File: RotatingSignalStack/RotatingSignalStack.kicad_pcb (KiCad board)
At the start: 2 copper layers, 4.1 x 4.1 mm, 94 parts, among them IC2 STM32H562RIT6, J2 Conn_ARM_SWD_TagConnect_TC203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, J3 RJ45_LED_Shielded, SW1 SW_Push, SW2 Boot Switch, SW3 SW_Push, SW4 SW_Push, SW8 SW_Push, T1 GMG116S1202R, U1 TMAG5273C1QDBVR, U2 AP63203WU-7, U3 SN65HVD232, U4 DP83825I, U5 SG-210STF 50.0000ML0, U6 USBLC6-2SC6, U7 USBLC6-4SC6

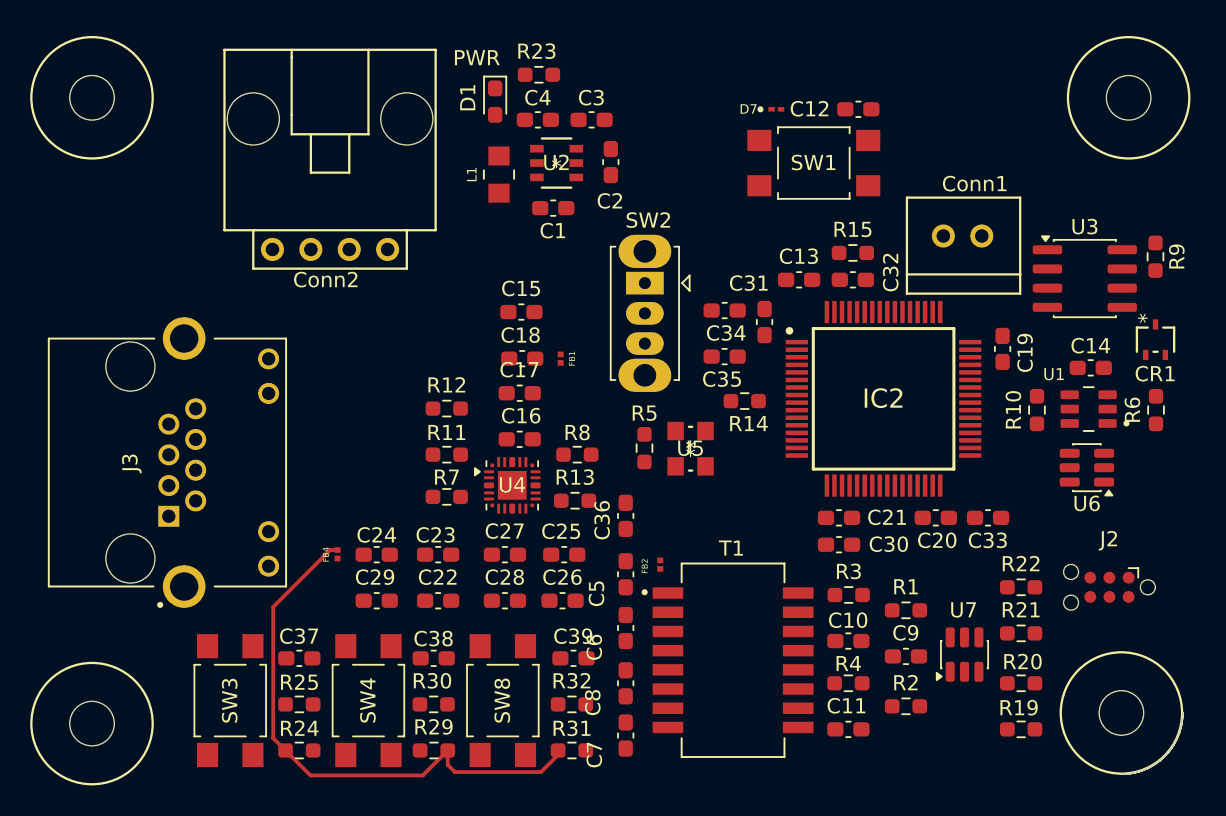
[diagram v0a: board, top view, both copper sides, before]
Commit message: mounting hole fix
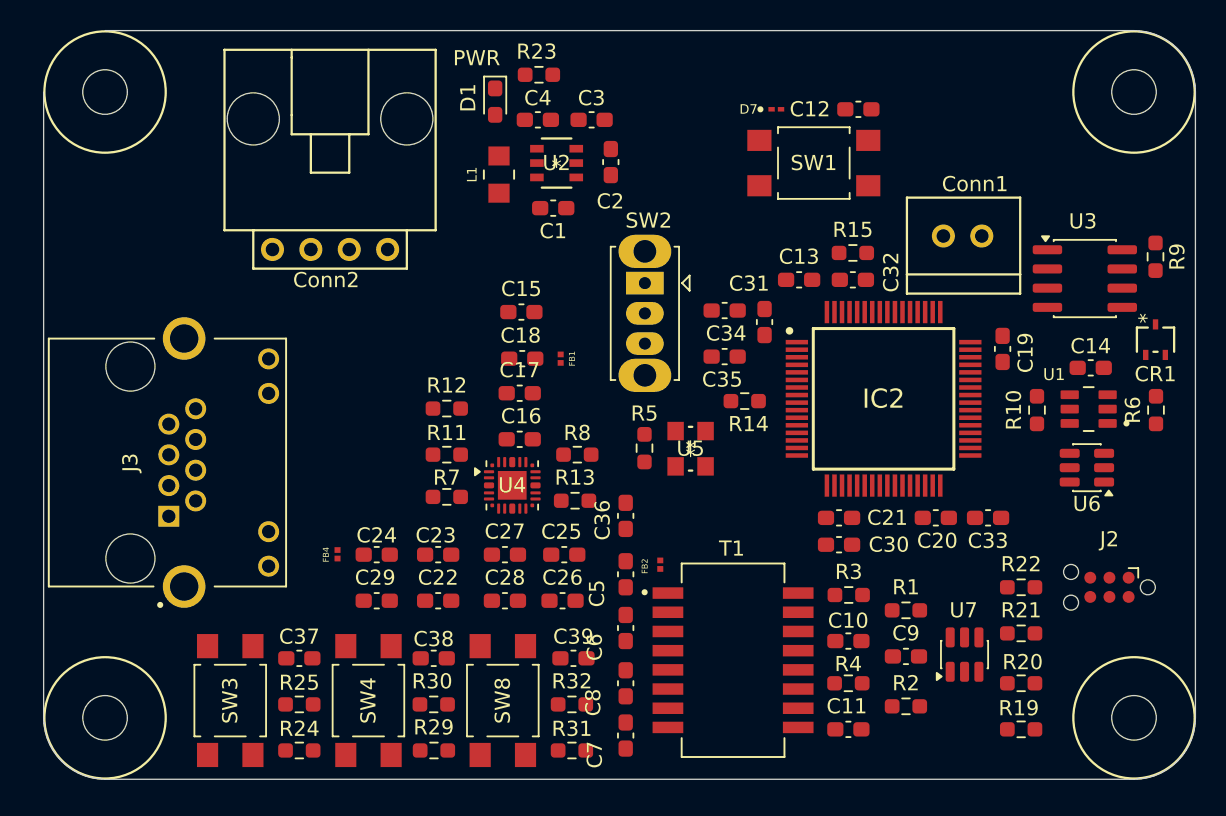
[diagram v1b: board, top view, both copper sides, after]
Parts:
- moved H1 69.3 mm to (179.9, 115.1), turned to -90 degrees
- moved H4 59.2 mm to (119.8, 115.1), turned to 180 degrees
- moved H2 33.8 mm to (119.8, 81.7), turned to 90 degrees
- moved H3 0.52 mm to (179.9, 81.7)
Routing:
- net VBAT: track 37.0 -> 0.29 mm
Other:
- board size 4.1 x 4.1 mm -> 76.2 x 49.5 mm
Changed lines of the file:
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@@
 	(footprint "MRDT_Drill_Holes:4_40_Hole_Corner"
 		(layer "F.Cu")
-		(at 118.96962 82.11312 90)
+		(at 179.88788 115.11788 -90)
 		(property "Reference" "H1"
 			(at 4.00812 -3.50812 90)
@@
 		)
 		(fp_line
-			(start 4.0132 -8.0264)
-			(end 0 -8.0264)
+			(start 0 0)
+			(end 8.0264 0)
 			(stroke
 				(width 0.15)
@@
 		)
 		(fp_line
-			(start 0 -8.0264)
-			(end 0 0)
+			(start 8.0264 -4.0132)
+			(end 8.0264 0)
 			(stroke
 				(width 0.15)
@@
 		)
 		(fp_line
-			(start 8.0264 -4.0132)
-			(end 8.0264 0)
+			(start 0 -8.0264)
+			(end 0 0)
 			(stroke
 				(width 0.15)
@@
 		)
 		(fp_line
-			(start 0 0)
-			(end 8.0264 0)
+			(start 4.0132 -8.0264)
+			(end 0 -8.0264)
 			(stroke
 				(width 0.15)
@@
 		)
 		(pad "" np_thru_hole circle
-			(at 4.00812 -4.00812 90)
+			(at 4.00812 -4.00812 270)
 			(size 2.9464 2.9464)
 			(drill 2.9464)
@@
 		)
 		(fp_text user "${REFERENCE}"
-			(at -1.524 -4.9295 90)
+			(at -0.1005 0 180)
 			(layer "F.Fab")
 			(effects
@@
 		(tags "SOIC SO")
 		(property "Reference" "U3"
-			(at 0 -3.4 0)
+			(at -0.127 -3.781 0)
 			(layer "F.SilkS")
 			(effects
@@
 	(footprint "MRDT_Drill_Holes:4_40_Hole_Corner"
 		(layer "F.Cu")
-		(at 179.53338 82.11312)
+		(at 179.88788 81.73212)
 		(property "Reference" "H3"
 			(at 4.00812 -3.50812 0)
@@
 	(footprint "MRDT_Drill_Holes:4_40_Hole_Corner"
 		(layer "F.Cu")
-		(at 179.0559 114.7939 -90)
+		(at 119.83212 115.11788 180)
 		(property "Reference" "H4"
-			(at 4.00812 -3.50812 90)
+			(at 4.00812 -3.50812 0)
 			(layer "F.SilkS")
 			(hide yes)
@@
 		)
 		(property "Value" "MountingHole"
-			(at 4.00812 -4.50812 90)
+			(at 4.00812 -4.50812 0)
 			(layer "F.Fab")
 			(hide yes)
@@
 		)
 		(property "Datasheet" "~"
-			(at 0 0 90)
+			(at 0 0 0)
 			(layer "F.Fab")
 			(hide yes)
@@
 		)
 		(property "Description" "Mounting Hole without connection"
-			(at 0 0 90)
+			(at 0 0 0)
 			(layer "F.Fab")
 			(hide yes)
@@
 		)
 		(fp_line
-			(start 0 0)
+			(start 8.0264 -4.0132)
 			(end 8.0264 0)
 			(stroke
@@
 		)
 		(fp_line
-			(start 8.0264 -4.0132)
-			(end 8.0264 0)
+			(start 4.0132 -8.0264)
+			(end 0 -8.0264)
 			(stroke
 				(width 0.15)
@@
 		)
 		(fp_line
-			(start 0 -8.0264)
-			(end 0 0)
+			(start 0 0)
+			(end 8.0264 0)
 			(stroke
 				(width 0.15)
@@
 		)
 		(fp_line
-			(start 4.0132 -8.0264)
-			(end 0 -8.0264)
+			(start 0 -8.0264)
+			(end 0 0)
 			(stroke
 				(width 0.15)
@@
 		)
 		(pad "" np_thru_hole circle
-			(at 4.00812 -4.00812 270)
+			(at 4.00812 -4.00812 180)
 			(size 2.9464 2.9464)
 			(drill 2.9464)
@@
 	(footprint "MRDT_Drill_Holes:4_40_Hole_Corner"
 		(layer "F.Cu")
-		(at 118.96962 115.49888 180)
+		(at 119.83212 81.73212 90)
 		(property "Reference" "H2"
-			(at 4.00812 -3.50812 0)
+			(at 4.00812 -3.50812 90)
 			(layer "F.SilkS")
 			(hide yes)
@@
 		)
 		(property "Value" "MountingHole"
-			(at 4.00812 -4.50812 0)
+			(at 4.00812 -4.50812 90)
 			(layer "F.Fab")
 			(hide yes)
@@
 		)
 		(property "Datasheet" "~"
-			(at 0 0 0)
+			(at 0 0 90)
 			(layer "F.Fab")
 			(hide yes)
@@
 		)
 		(property "Description" "Mounting Hole without connection"
-			(at 0 0 0)
+			(at 0 0 90)
 			(layer "F.Fab")
 			(hide yes)
@@
 		)
 		(fp_line
-			(start 8.0264 -4.0132)
-			(end 8.0264 0)
+			(start 4.0132 -8.0264)
+			(end 0 -8.0264)
 			(stroke
 				(width 0.15)
@@
 		)
 		(fp_line
-			(start 4.0132 -8.0264)
-			(end 0 -8.0264)
+			(start 0 -8.0264)
+			(end 0 0)
 			(stroke
 				(width 0.15)
@@
 		)
 		(fp_line
-			(start 0 0)
+			(start 8.0264 -4.0132)
 			(end 8.0264 0)
 			(stroke
@@
 		)
 		(fp_line
-			(start 0 -8.0264)
-			(end 0 0)
+			(start 0 0)
+			(end 8.0264 0)
 			(stroke
 				(width 0.15)
@@
 		)
 		(pad "" np_thru_hole circle
-			(at 4.00812 -4.00812 180)
+			(at 4.00812 -4.00812 90)
 			(size 2.9464 2.9464)
 			(drill 2.9464)
@@
 	)
 	(gr_arc
-		(start 187.12802 118.80202)
-		(mid 185.937702 121.675702)
-		(end 183.06402 122.86602)
+		(start 115.824 123.19)
+		(mid 112.950318 121.999682)
+		(end 111.76 119.126)
 		(stroke
 			(width 0.05)
@@
 	)
 	(gr_arc
-		(start 187.12802 118.80202)
-		(mid 185.937702 121.675702)
-		(end 183.06402 122.86602)
+		(start 183.896 73.66)
+		(mid 186.769682 74.850318)
+		(end 187.96 77.724)
 		(stroke
 			(width 0.05)
@@
 		(layer "Edge.Cuts")
 	)
-	(gr_arc
-		(start 187.12802 118.80202)
-		(mid 185.937702 121.675702)
-		(end 183.06402 122.86602)
+	(gr_line
+		(start 115.824 123.19)
+		(end 183.896 123.19)
+		(stroke
+			(width 0.05)
+			(type default)
+		)
+		(layer "Edge.Cuts")
+	)
+	(gr_line
+		(start 183.896 73.66)
+		(end 115.824 73.66)
+		(stroke
+			(width 0.05)
+			(type default)
+		)
+		(layer "Edge.Cuts")
+	)
+	(gr_line
+		(start 187.96 119.126)
+		(end 187.96 77.724)
+		(stroke
+			(width 0.05)
+			(type default)
+		)
+		(layer "Edge.Cuts")
+	)
+	(gr_line
+		(start 111.76 77.724)
+		(end 111.76 119.126)
 		(stroke
 			(width 0.05)
@@
 	)
 	(gr_arc
-		(start 187.12802 118.80202)
-		(mid 185.937702 121.675702)
-		(end 183.06402 122.86602)
+		(start 187.96 119.126)
+		(mid 186.769682 121.999682)
+		(end 183.896 123.19)
 		(stroke
 			(width 0.05)
@@
 	)
 	(segment
-		(start 145.799 121.5795)
-		(end 144.6675 122.711)
-		(width 0.254)
-		(layer "F.Cu")
-		(net 6)
-	)
-	(segment
-		(start 138.495224 122.239224)
-		(end 138.495224 121.285)
-		(width 0.254)
-		(layer "F.Cu")
-		(net 6)
-	)
-	(segment
-		(start 126.9495 120.4695)
-		(end 126.9495 111.7935)
-		(width 0.254)
-		(layer "F.Cu")
-		(net 6)
-	)
-	(segment
-		(start 127.765 121.285)
-		(end 126.9495 120.4695)
-		(width 0.254)
-		(layer "F.Cu")
-		(net 6)
-	)
-	(segment
-		(start 129.416 122.936)
-		(end 127.765 121.285)
-		(width 0.254)
-		(layer "F.Cu")
-		(net 6)
-	)
-	(segment
-		(start 138.967 122.711)
-		(end 138.495224 122.239224)
-		(width 0.254)
-		(layer "F.Cu")
-		(net 6)
-	)
-	(segment
-		(start 136.844224 122.936)
-		(end 129.416 122.936)
-		(width 0.254)
-		(layer "F.Cu")
-		(net 6)
-	)
-	(segment
-		(start 138.495224 121.285)
-		(end 136.844224 122.936)
-		(width 0.254)
-		(layer "F.Cu")
-		(net 6)
-	)
-	(segment
 		(start 145.799 121.285)
 		(end 145.799 121.5795)
 		(width 0.254)
 		(layer "F.Cu")
-		(net 6)
-	)
-	(segment
-		(start 144.6675 122.711)
-		(end 138.967 122.711)
-		(width 0.254)
-		(layer "F.Cu")
-		(net 6)
-	)
-	(segment
-		(start 130.72 108.023)
-		(end 131.204 108.023)
-		(width 0.254)
-		(layer "F.Cu")
-		(net 6)
-	)
-	(segment
-		(start 126.9495 111.7935)
-		(end 130.72 108.023)
-		(width 0.254)
-		(layer "F.Cu")

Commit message: placement fix
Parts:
- removed C21, C38, C39: 100nF, Capacitor_SMD:C_0603_1608Metric_Pad1.08x0.95mm_HandSolder
- removed Conn2: Molex_SL_04, MRDT_Connectors:MOLEX_SL_04_Horizontal
- removed J2: Conn_ARM_SWD_TagConnect_TC2030-NL, Connector:Tag-Connect_TC2030-IDC-NL_2x03_P1.27mm_Vertical
- removed R25, R30, R32: 100, Resistor_SMD:R_0603_1608Metric_Pad0.98x0.95mm_HandSolder
- removed R29, R31: 4.7k, Resistor_SMD:R_0603_1608Metric_Pad0.98x0.95mm_HandSolder
- removed SW3, SW4, SW8: SW_Push, Button_Switch_SMD:SW_SPST_TL3305A
- added D10: Orange, LED_SMD:LED_0603_1608Metric_Pad1.05x0.95mm_HandSolder, F.Cu at (167.9, 98.8)
- added D2: RED, LED_SMD:LED_0603_1608Metric_Pad1.05x0.95mm_HandSolder, F.Cu at (193.5, 85.8)
- added D3: Orange, LED_SMD:LED_0603_1608Metric_Pad1.05x0.95mm_HandSolder, F.Cu at (178.1, 98.8)
- added D9: Orange, LED_SMD:LED_0603_1608Metric_Pad1.05x0.95mm_HandSolder, F.Cu at (178.0, 109.2)
- added J1: Conn_ARM_SWD_TagConnect_TC2030-NL, Connector:Tag-Connect_TC2030-IDC-NL_2x03_P1.27mm_Vertical, F.Cu at (156.5, 103.3)
- added R16: 6.8k, Resistor_SMD:R_0603_1608Metric_Pad0.98x0.95mm_HandSolder, F.Cu at (192.1, 89.5)
- added R17: 1k, Resistor_SMD:R_0603_1608Metric_Pad0.98x0.95mm_HandSolder, F.Cu at (183.8, 109.2)
- added R18: 1k, Resistor_SMD:R_0603_1608Metric_Pad0.98x0.95mm_HandSolder, F.Cu at (183.8, 98.8)
- added SW5: SW_Push, Button_Switch_SMD:SW_SPST_TL3305A, F.Cu at (180.9, 95.2)
- added SW6: SW_Push, Button_Switch_SMD:SW_SPST_TL3305A, F.Cu at (180.9, 105.7)
- added SW7: SW_Push, Button_Switch_SMD:SW_SPST_TL3305A, F.Cu at (170.7, 95.2)
- C12, C13, C17, C19, C2, C20, C23, C31, C35: value 100nF -> 0.1uF
- C30: value 4.7nF -> 4.7uF
- C33: value 2.2uF -> 0.1uF
- C37: value 100nF -> 22uF
- C4: value 22uF -> 2.2uF
- Conn1: value Molex_uF_D_02 -> Molex_SL_04; footprint MRDT_Connectors:MOLEX_SL_02_Vertical -> MRDT_Connectors:MOLEX_SL_04_Horizontal
- R24: value 4.7k -> 1k
- moved H4 82.9 mm to (196.7, 84.0), turned to 0 degrees
- moved J3 81.0 mm to (198.1, 110.5), turned to 90 degrees
- moved C37 74.2 mm to (199.7, 93.6), turned to -90 degrees
- moved L1 57.2 mm to (196.9, 99.0), turned to 0 degrees
- moved D1 55.8 mm to (196.9, 85.8)
- moved H1 53.8 mm to (136.0, 83.9), turned to 90 degrees
- moved R23 52.2 mm to (195.1, 89.5), turned to 90 degrees
- moved C3 51.8 mm to (197.9, 93.6), turned to -90 degrees
- moved U2 50.6 mm to (195.1, 93.6), turned to -90 degrees
- moved R24 50.3 mm to (173.6, 98.8), turned to 180 degrees
- moved C2 49.3 mm to (196.4, 96.7), turned to 180 degrees
- moved C1 47.3 mm to (192.1, 93.7), turned to -90 degrees
- moved H3 42.2 mm to (196.7, 120.5), turned to -90 degrees
- moved H2 42.1 mm to (136.1, 120.5), turned to 180 degrees
- moved R6 35.2 mm to (151.4, 89.7), turned to 0 degrees
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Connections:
- net /Connectors/NRST renamed /STM/NRST
- C13 pad 2: Net-(C13-Pad2) -> VSSA
- C19 pad 1: Net-(C13-Pad2) -> VBAT
- C19 pad 2: Net-(C19-Pad2) -> VSSA
- C20 pad 1: Net-(C19-Pad2) -> VBAT
- C20 pad 2: Net-(C20-Pad2) -> VSSA
- C3 pad 2: Net-(C3-Pad2) -> VSSA
- C32 pad 1: Net-(C32-Pad1) -> VSSA
- C33 pad 1: VSSA -> VBAT
- C33 pad 2: Net-(C32-Pad1) -> VSSA
- C37 pad 1: /Buttons/JOG A -> VBAT
- C37 pad 2: Net-(C37-Pad2) -> VSSA
- C4 pad 1: Net-(C3-Pad2) -> VSSA
- C4 pad 2: VSSA -> VCAP1
- Conn1 pad 1: /CAN/CANH -> VBUS
- Conn1 pad 2: /CAN/CANL -> VSSA
- IC2 pad 46: /Connectors/SWDIO -> /STM/SWDIO
- IC2 pad 49: /Connectors/SWDCLK -> /STM/SWCLK
- IC2 pad 55: /Connectors/SWO -> /STM/SWO
- J3 pad 11: /Ethernet and Magnetics/LED2 -> VSSA
- J3 pad 12: VSSA -> /Ethernet and Magnetics/LED2
- R24 pad 1: VBAT -> /Buttons/JOG A
- R24 pad 2: /Buttons/JOG A -> Net-(D10-K)
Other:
- board outline removed
- board text added: "24V"
- board text added: "3v3"
- board text added: "ALIGN"
- board text added: "JOG A"
- board text added: "JOG B"
- board text added: "RESET"
- board text removed: "PWR"

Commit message: layout
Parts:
- removed J1: Conn_ARM_SWD_TagConnect_TC2030-NL, Connector:Tag-Connect_TC2030-IDC-NL_2x03_P1.27mm_Vertical
- added J2: Conn_01x04, Connector_PinSocket_2.54mm:PinSocket_1x04_P2.54mm_Vertical, F.Cu at (134.1, 68.1)
- moved J3 62.5 mm to (142.5, 138.9), turned to 0 degrees
- moved C10 61.2 mm to (131.6, 133.7), turned to 90 degrees
- moved R3 56.9 mm to (131.6, 130.0), turned to 90 degrees
- moved C11 51.1 mm to (153.4, 133.6), turned to 90 degrees
- moved R1 50.6 mm to (134.3, 105.4), turned to 90 degrees
- moved C9 48.2 mm to (137.6, 105.4), turned to -90 degrees
- moved R2 46.4 mm to (140.6, 105.4), turned to 90 degrees
- moved R4 46.1 mm to (153.4, 130.0), turned to 90 degrees
- moved H4 45.5 mm to (154.7, 66.2)
- moved H3 45.0 mm to (154.7, 137.0)
- moved C37 43.1 mm to (157.1, 87.3), turned to 180 degrees
- moved C2 42.6 mm to (157.2, 79.9), turned to 0 degrees
- moved U2 42.6 mm to (154.0, 82.5), turned to 0 degrees
- moved R13 42.3 mm to (125.5, 93.9), turned to 90 degrees
- moved C3 41.7 mm to (157.1, 85.5), turned to 180 degrees
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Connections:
- net /STM/NRST renamed Net-(IC2-NRST)
- IC2 pad 46: /STM/SWDIO -> SWDIO
- IC2 pad 49: /STM/SWCLK -> SWDCLK
- IC2 pad 55: /STM/SWO -> unconnected-(IC2-PB3-Pad55)
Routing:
- net VBAT: track 0.00 -> 55.1 mm, vias 0 -> 1
- net VBUS: track 0.00 -> 14.3 mm
- net Net-(IC2-NRST): track 0.00 -> 5.32 mm
- net Net-(U2-SW): track 0.00 -> 5.14 mm
- net VCAP1: track 0.00 -> 3.85 mm
- net Net-(D2-K): track 0.00 -> 3.10 mm
- net Net-(D1-K): track 0.00 -> 3.06 mm
- net Net-(U2-BST): track 0.00 -> 2.04 mm
- net /Oscillator/STM_CLK_IN: track 0.00 -> 0.90 mm
- added copper zone on B.Cu, net VSSA
- added copper zone on F.Cu, net VSSA
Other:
- board outline added: 41.1 x 86.9 mm
- board text added: "BOOT"

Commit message: evil layout
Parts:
- moved R7 35.7 mm to (131.6, 127.3), turned to 180 degrees
- moved C9 32.1 mm to (155.2, 132.2)
- moved R1 31.1 mm to (157.0, 126.7), turned to -90 degrees
- moved R11 30.1 mm to (145.9, 127.3), turned to 0 degrees
- moved R2 29.8 mm to (157.0, 130.3)
- moved R13 20.8 mm to (144.0, 103.5), turned to 180 degrees
- moved R8 18.7 mm to (144.0, 100.4), turned to 180 degrees
- moved C36 18.3 mm to (132.6, 109.7)
- moved R22 18.2 mm to (141.5, 109.5), turned to 90 degrees
- moved FB2 16.6 mm to (134.9, 110.5), turned to 90 degrees
- moved R19 16.3 mm to (136.1, 109.5), turned to 90 degrees
- moved R21 15.8 mm to (139.7, 109.5), turned to 90 degrees
- moved FB1 15.8 mm to (142.7, 91.2)
- moved C25 14.7 mm to (141.5, 105.9), turned to 90 degrees
- moved R20 14.2 mm to (137.9, 109.5), turned to 90 degrees
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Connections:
- C25 pad 1: Tx+ -> /Ethernet and Magnetics/Tx+
- C26 pad 1: Tx- -> /Ethernet and Magnetics/Tx-
- C27 pad 1: Rx+ -> /Ethernet and Magnetics/Rx+
- C28 pad 1: Rx- -> /Ethernet and Magnetics/Rx-
- J3 pad 1: Tx+ -> Net-(J3-Pad1)
- J3 pad 2: Tx- -> Net-(J3-Pad2)
- J3 pad 3: Rx+ -> Net-(J3-Pad3)
- J3 pad 6: Rx- -> Net-(J3-Pad6)
- R19 pad 2: Rx- -> /Ethernet and Magnetics/Rx-
- R20 pad 2: Rx+ -> /Ethernet and Magnetics/Rx+
- R21 pad 2: Tx- -> /Ethernet and Magnetics/Tx-
- R22 pad 2: Tx+ -> /Ethernet and Magnetics/Tx+
- T1 pad 1: Tx+ -> /Ethernet and Magnetics/Tx+
- T1 pad 11: Rx+ -> Net-(J3-Pad3)
- T1 pad 14: Tx- -> Net-(J3-Pad2)
- T1 pad 16: Tx+ -> Net-(J3-Pad1)
- T1 pad 3: Tx- -> /Ethernet and Magnetics/Tx-
- T1 pad 6: Rx+ -> /Ethernet and Magnetics/Rx+
- T1 pad 8: Rx- -> /Ethernet and Magnetics/Rx-
- T1 pad 9: Rx- -> Net-(J3-Pad6)
- U7 pad 1: Rx- -> /Ethernet and Magnetics/Rx-
- U7 pad 3: Rx+ -> /Ethernet and Magnetics/Rx+
- U7 pad 4: Tx- -> /Ethernet and Magnetics/Tx-
- U7 pad 6: Tx+ -> /Ethernet and Magnetics/Tx+
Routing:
- net Net-(IC2-NRST): track 5.32 -> 128.4 mm
- net VBUS: track 14.3 -> 95.3 mm, vias 0 -> 1
- net VBAT: track 55.1 -> 133.0 mm, vias 1 -> 8
- net /Buttons/JOG B: track 0.00 -> 69.3 mm
- net /Buttons/JOG A: track 0.00 -> 68.8 mm
- net /Buttons/ALIGN: track 0.00 -> 55.2 mm, vias 0 -> 1
- net Net-(SW2-B): track 0.00 -> 46.3 mm, vias 0 -> 3
- net /PHY/MDC: track 0.00 -> 34.3 mm
- net GNDPWR: track 0.00 -> 33.6 mm
- net /Compass/I2C3_SCL: track 0.00 -> 33.3 mm, vias 0 -> 1
- net /PHY/MDIO: track 0.00 -> 32.7 mm, vias 0 -> 1
- net Net-(U4-50MHzOut/LED2/S(RX_DV_EN)): track 0.00 -> 31.7 mm, vias 0 -> 1
- net Net-(J3-Pad3): track 0.00 -> 28.6 mm
- net /PHY/RST: track 0.00 -> 26.5 mm
- net /PHY/RX_D1: track 0.00 -> 25.5 mm
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
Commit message: new one
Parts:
- D1, D2: value RED -> GREEN
- moved H2 75.4 mm to (112.0, 63.7), turned to 90 degrees
- moved R7 60.8 mm to (170.2, 80.3), turned to 0 degrees
- moved R2 55.6 mm to (121.4, 87.5)
- moved J3 54.5 mm to (114.6, 92.1), turned to 90 degrees
- moved R11 54.4 mm to (178.9, 84.0)
- moved H3 54.4 mm to (197.9, 103.9)
- moved C30 53.6 mm to (179.4, 64.3), turned to -90 degrees
- moved D10 52.1 mm to (117.1, 68.6), turned to 180 degrees
- moved D9 52.1 mm to (137.5, 68.6), turned to 180 degrees
- moved SW6 51.1 mm to (140.3, 65.1), turned to 0 degrees
- moved D3 51.0 mm to (127.2, 68.6), turned to 180 degrees
- moved SW1 50.8 mm to (150.4, 65.1), turned to 180 degrees
- moved C10 49.9 mm to (128.1, 83.9), turned to 0 degrees
- moved J2 49.7 mm to (182.9, 59.2), turned to 90 degrees
- moved SW7 48.5 mm to (119.9, 65.1), turned to 0 degrees
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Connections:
- IC2 pad 3: unconnected-(IC2-PC14-OSC32_IN-Pad3) -> /Buttons/JOG B
- IC2 pad 4: unconnected-(IC2-PC15-OSC32_OUT-Pad4) -> /Buttons/JOG A
- IC2 pad 51: /Buttons/ALIGN -> unconnected-(IC2-PC10-Pad51)
- IC2 pad 52: /Buttons/JOG A -> unconnected-(IC2-PC11-Pad52)
- IC2 pad 53: /Buttons/JOG B -> unconnected-(IC2-PC12-Pad53)
- IC2 pad 6: unconnected-(IC2-PH1-OSC_OUT-Pad6) -> /Buttons/ALIGN
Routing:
- net VBAT: track 133.0 -> 0.00 mm, vias 8 -> 0
- net Net-(IC2-NRST): track 128.4 -> 0.00 mm
- net VBUS: track 95.3 -> 0.00 mm, vias 1 -> 0
- net /Buttons/JOG B: track 69.3 -> 0.00 mm
- net /Buttons/JOG A: track 68.8 -> 0.00 mm
- net /Buttons/ALIGN: track 55.2 -> 0.00 mm, vias 1 -> 0
- net Net-(SW2-B): track 46.3 -> 0.00 mm, vias 3 -> 0
- net /PHY/MDC: track 34.3 -> 0.00 mm
- net GNDPWR: track 33.6 -> 0.00 mm
- net /Compass/I2C3_SCL: track 33.3 -> 0.00 mm, vias 1 -> 0
- net /PHY/MDIO: track 32.7 -> 0.00 mm, vias 1 -> 0
- net Net-(U4-50MHzOut/LED2/S(RX_DV_EN)): track 31.7 -> 0.00 mm, vias 1 -> 0
- net Net-(J3-Pad3): track 28.6 -> 0.00 mm
- net /PHY/RST: track 26.5 -> 0.00 mm
- net /PHY/RX_D1: track 25.5 -> 0.00 mm
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- added copper zone on B.Cu, net GNDPWR
- added copper zone on F.Cu, net GNDPWR
- removed copper zone on B.Cu, net VSSA
- removed copper zone on F.Cu, net VSSA
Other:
- board size 41.1 x 86.9 mm -> 102.1 x 56.4 mm
